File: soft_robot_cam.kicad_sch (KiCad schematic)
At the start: 76 parts, among them J1 Connector, J10 Screw_Terminal_01x02, J2 Conn_01x06, J3 Conn_01x03, J4 Conn_01x05_Pin, J5 Screw_Terminal_01x04, J6 Screw_Terminal_01x02, J7 Screw_Terminal_01x02, J8 Conn_01x24_Socket, J9 Screw_Terminal_01x02, Q1 S8050, Q2 S8050, Q3 AO3401A, SW1 SW_DIP_x02, SW3 SW_DP3T, SW4 SW_DIP_x02, SW5 SW_DP3T, U10 ICM-42605, U12 XC6206P282MR, U13 XC6206P122MR, U14 SY8113IADC, U3 MPU6500, U4 DRV8874PWPR, U5 DRV8874PWPR, U9 ESP32-S3-WROOM-1-N16R8

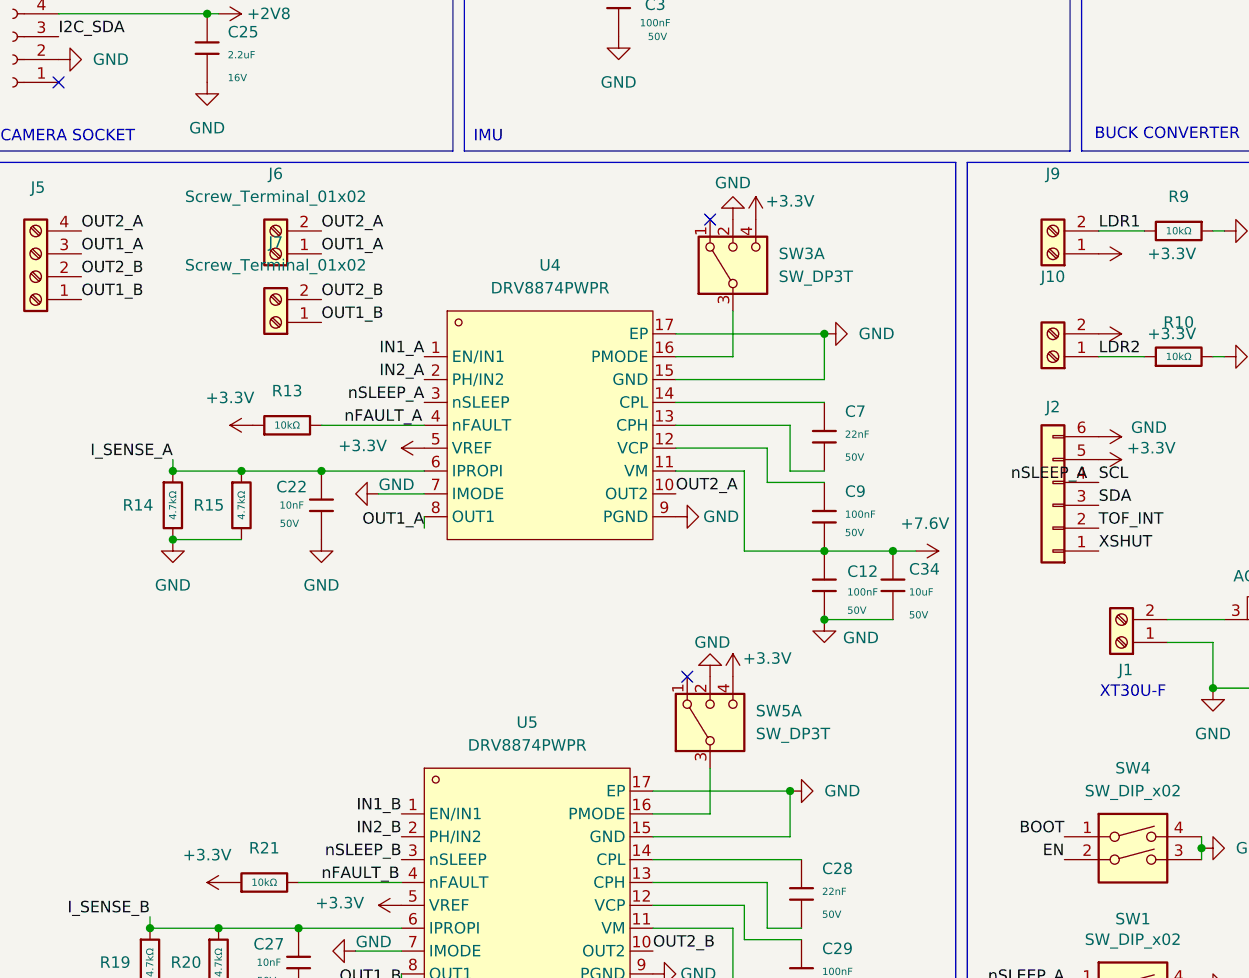
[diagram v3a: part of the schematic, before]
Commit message: Added most 3D models, revised some layout based off 3D model placement, need to verify JST-XH placement and ensure no design errors.
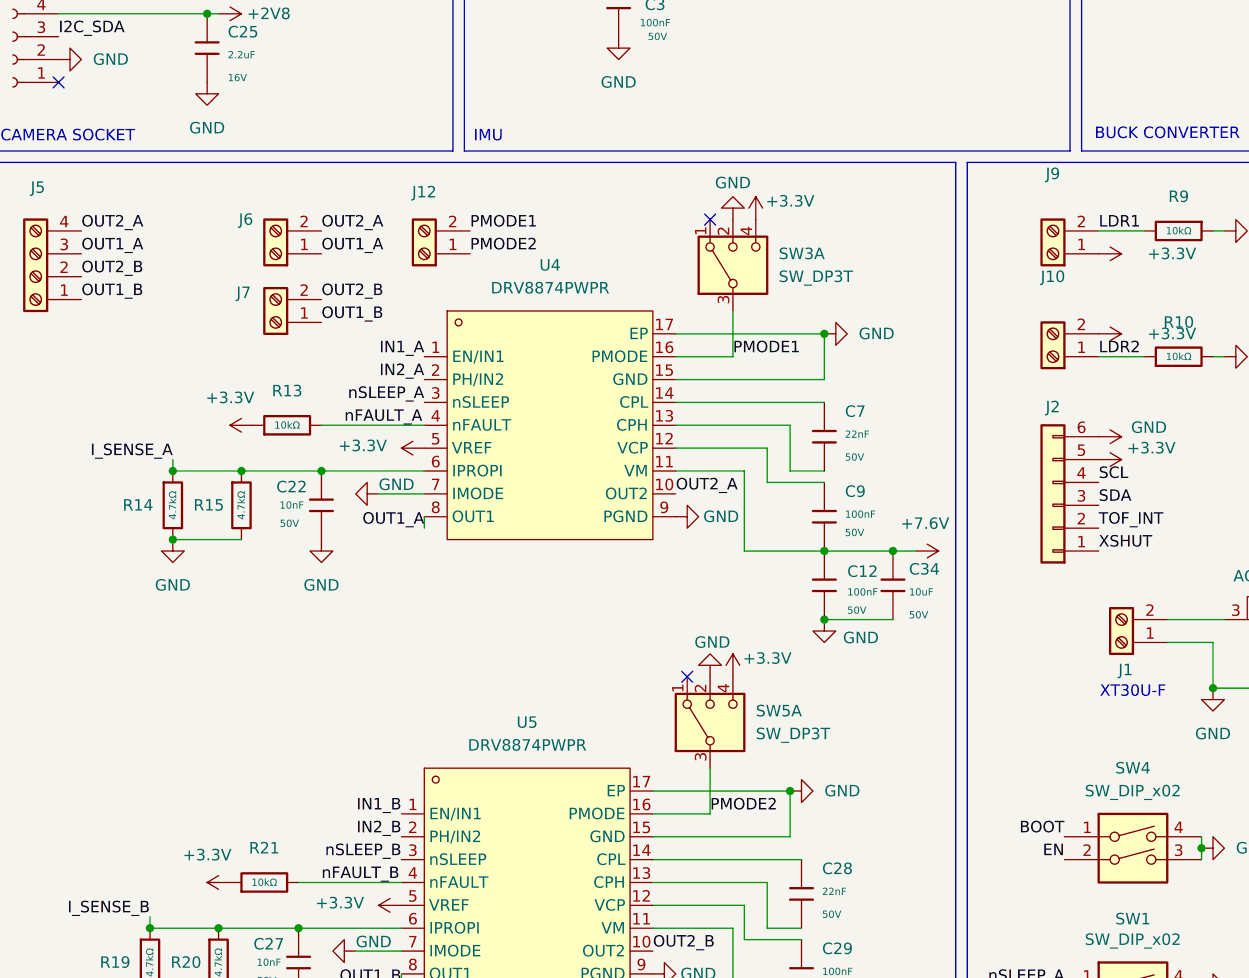
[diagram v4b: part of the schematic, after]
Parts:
- added J12: Screw_Terminal_01x02, Connector_PinHeader_1.00mm:PinHeader_1x02_P1.00mm_Vertical, symbol Connector:Screw_Terminal_01x02
- J1: LCSC (none) -> C99102
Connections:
- net PMODE1: now reaches SW3.3, U4.16 (PMODE)
- net PMODE1: now also J12.2 (Pin_2)
- net PMODE2: now reaches SW5.3, U5.16 (PMODE)
- net PMODE2: now also J12.1 (Pin_1)
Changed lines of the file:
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@@
 		)
 	)
+	(label "PMODE1"
+		(at 67.31 95.25 0)
+		(effects
+			(font
+				(size 1.27 1.27)
+			)
+			(justify left bottom)
+		)
+	)
 	(label "OUT1_B"
 		(at 59.69 179.07 180)
@@
 		)
 	)
+	(label "PMODE2"
+		(at 93.98 160.02 0)
+		(effects
+			(font
+				(size 1.27 1.27)
+			)
+			(justify left bottom)
+		)
+	)
 	(label "SCLK1"
 		(at 124.46 41.91 0)
@@
 		)
 	)
+	(label "PMODE1"
+		(at 96.52 109.22 0)
+		(effects
+			(font
+				(size 1.27 1.27)
+			)
+			(justify left bottom)
+		)
+	)
 	(label "HREF"
 		(at 220.98 111.76 180)
@@
 		)
 	)
-	(label "nSLEEP_A"
-		(at 135.89 123.19 180)
-		(effects
-			(font
-				(size 1.27 1.27)
-			)
-			(justify right bottom)
-		)
-	)
 	(label "BOOT"
 		(at 133.35 162.56 180)
@@
 		)
 	)
+	(label "PMODE2"
+		(at 67.31 97.79 0)
+		(effects
+			(font
+				(size 1.27 1.27)
+			)
+			(justify left bottom)
+		)
+	)
 	(label "Y3"
 		(at 21.59 27.94 0)
@@
 	)
 	(symbol
+		(lib_id "Connector:Screw_Terminal_01x02")
+		(at 62.23 97.79 180)
+		(unit 1)
+		(exclude_from_sim no)
+		(in_bom yes)
+		(on_board yes)
+		(dnp no)
+		(property "Reference" "J12"
+			(at 62.23 90.932 0)
+			(effects
+				(font
+					(size 1.27 1.27)
+				)
+			)
+		)
+		(property "Value" "Screw_Terminal_01x02"
+			(at 62.23 91.44 0)
+			(effects
+				(font
+					(size 1.27 1.27)
+				)
+				(hide yes)
+			)
+		)
+		(property "Footprint" "Connector_PinHeader_1.00mm:PinHeader_1x02_P1.00mm_Vertical"
+			(at 62.23 97.79 0)
+			(effects
+				(font
+					(size 1.27 1.27)
+				)
+				(hide yes)
+			)
+		)
+		(property "Datasheet" "~"
+			(at 62.23 97.79 0)
+			(effects
+				(font
+					(size 1.27 1.27)
+				)
+				(hide yes)
+			)
+		)
+		(property "Description" "Generic screw terminal, single row, 01x02, script generated (kicad-library-utils/schlib/autogen/connector/)"
+			(at 62.23 97.79 0)
+			(effects
+				(font
+					(size 1.27 1.27)
+				)
+				(hide yes)
+			)
+		)
+		(property "LCSC" ""
+			(at 62.23 97.79 0)
+			(effects
+				(font
+					(size 1.27 1.27)
+				)
+				(hide yes)
+			)
+		)
+		(pin "1"
+		)
+		(pin "2"
+		)
+		(instances
+			(project "soft_robot_cam"
+				(path "/8a7e5bec-e932-4403-8e68-78633cb41e92"
+					(reference "J12")
+					(unit 1)
+				)
+			)
+		)
+	)
+	(symbol
 		(lib_id "power:VD")
 		(at 163.83 119.38 270)
@@
 			)
 		)
+		(property "LCSC" "C99102"
+			(at 139.7 140.97 0)
+			(effects
+				(font
+					(size 1.27 1.27)
+				)
+				(hide yes)
+			)
+		)
 		(pin "1"
 		)
@@
 		(on_board yes)
 		(dnp no)
-		(fields_autoplaced yes)
 		(property "Reference" "J6"
-			(at 45.72 88.9 0)
+			(at 42.418 93.98 0)
 			(effects
 				(font
@@
 					(size 1.27 1.27)
 				)
+				(hide yes)
 			)
 		)
@@
 		(on_board yes)
 		(dnp no)
-		(fields_autoplaced yes)
 		(property "Reference" "J7"
-			(at 45.72 96.52 0)
+			(at 42.164 102.108 0)
 			(effects
 				(font
@@
 					(size 1.27 1.27)
 				)
+				(hide yes)
 			)
 		)

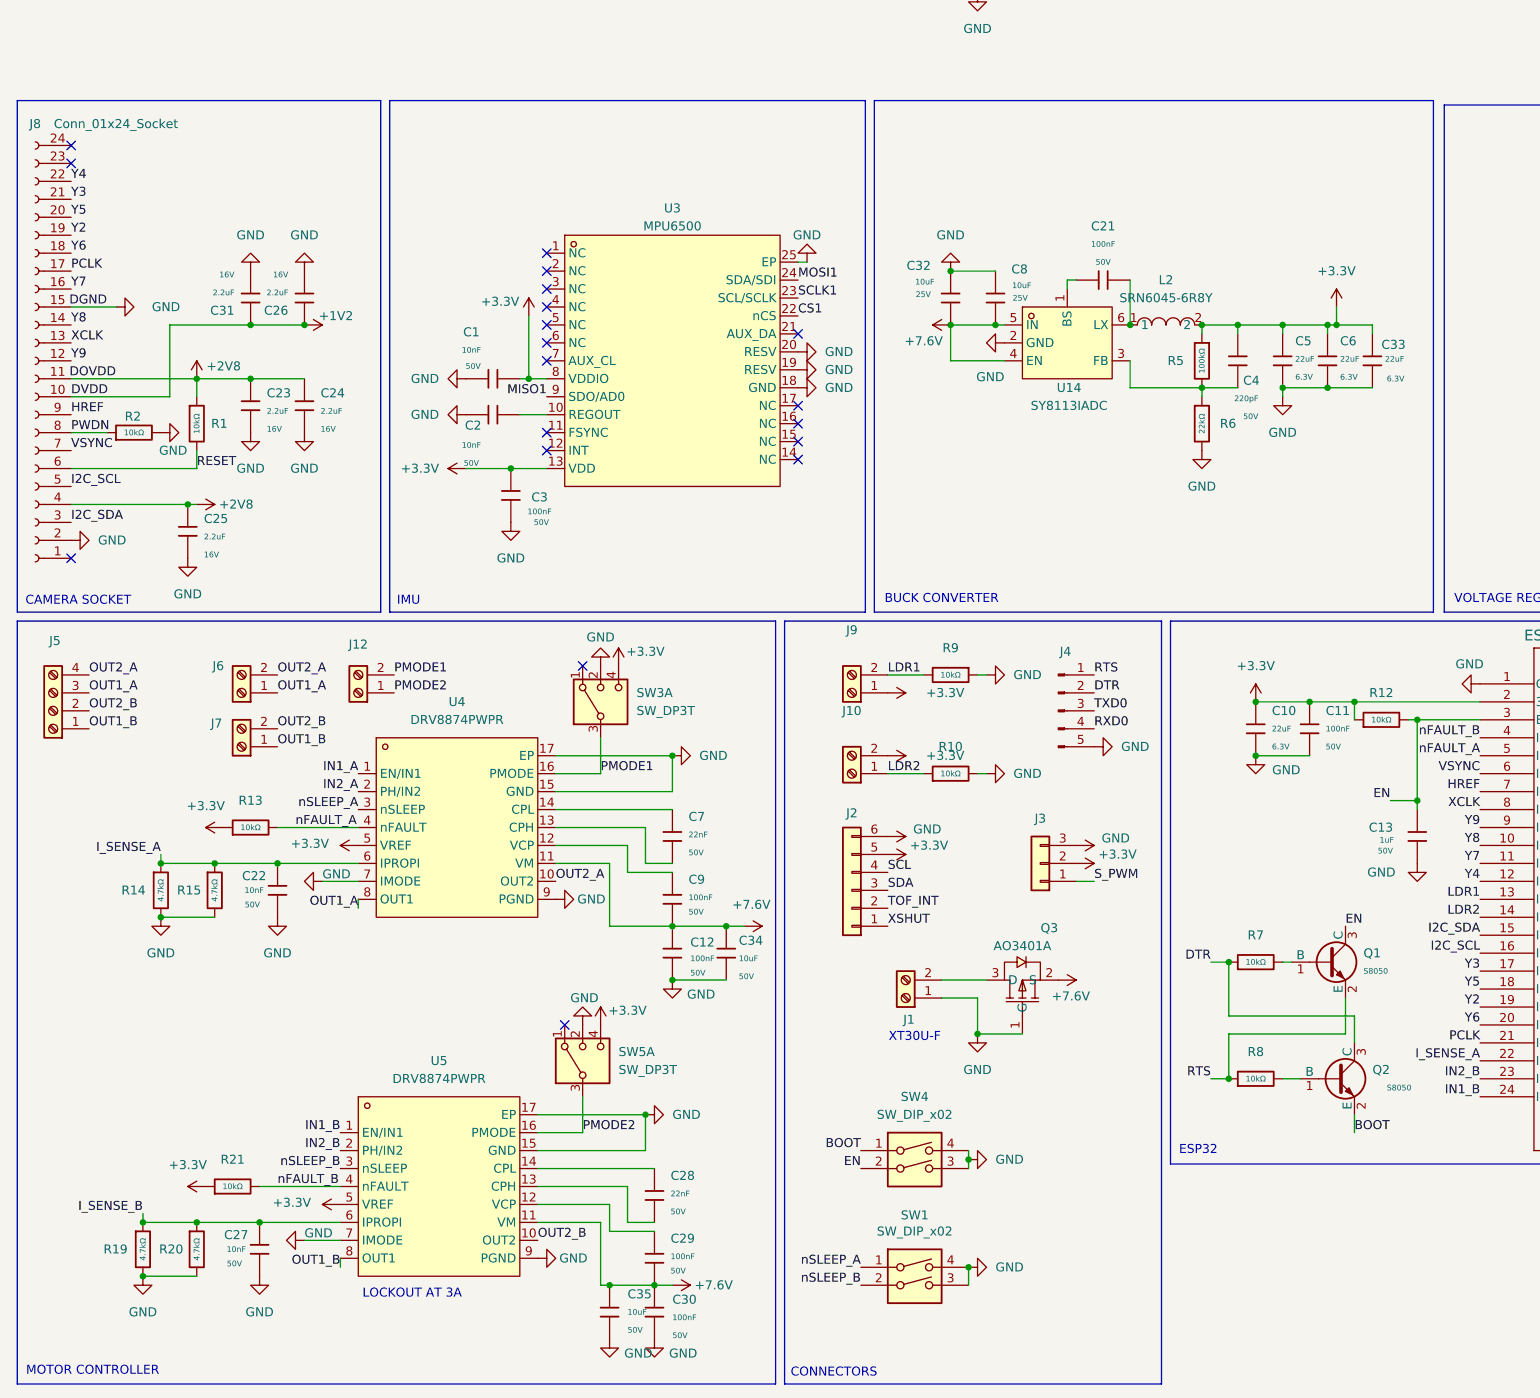
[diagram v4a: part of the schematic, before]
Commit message: Reviewed connector placement, chaning footprint to ensure clearance, added LEDs on Buck, slightly modified layout to improve spacing and clearance. Next is a full design and BOM review.
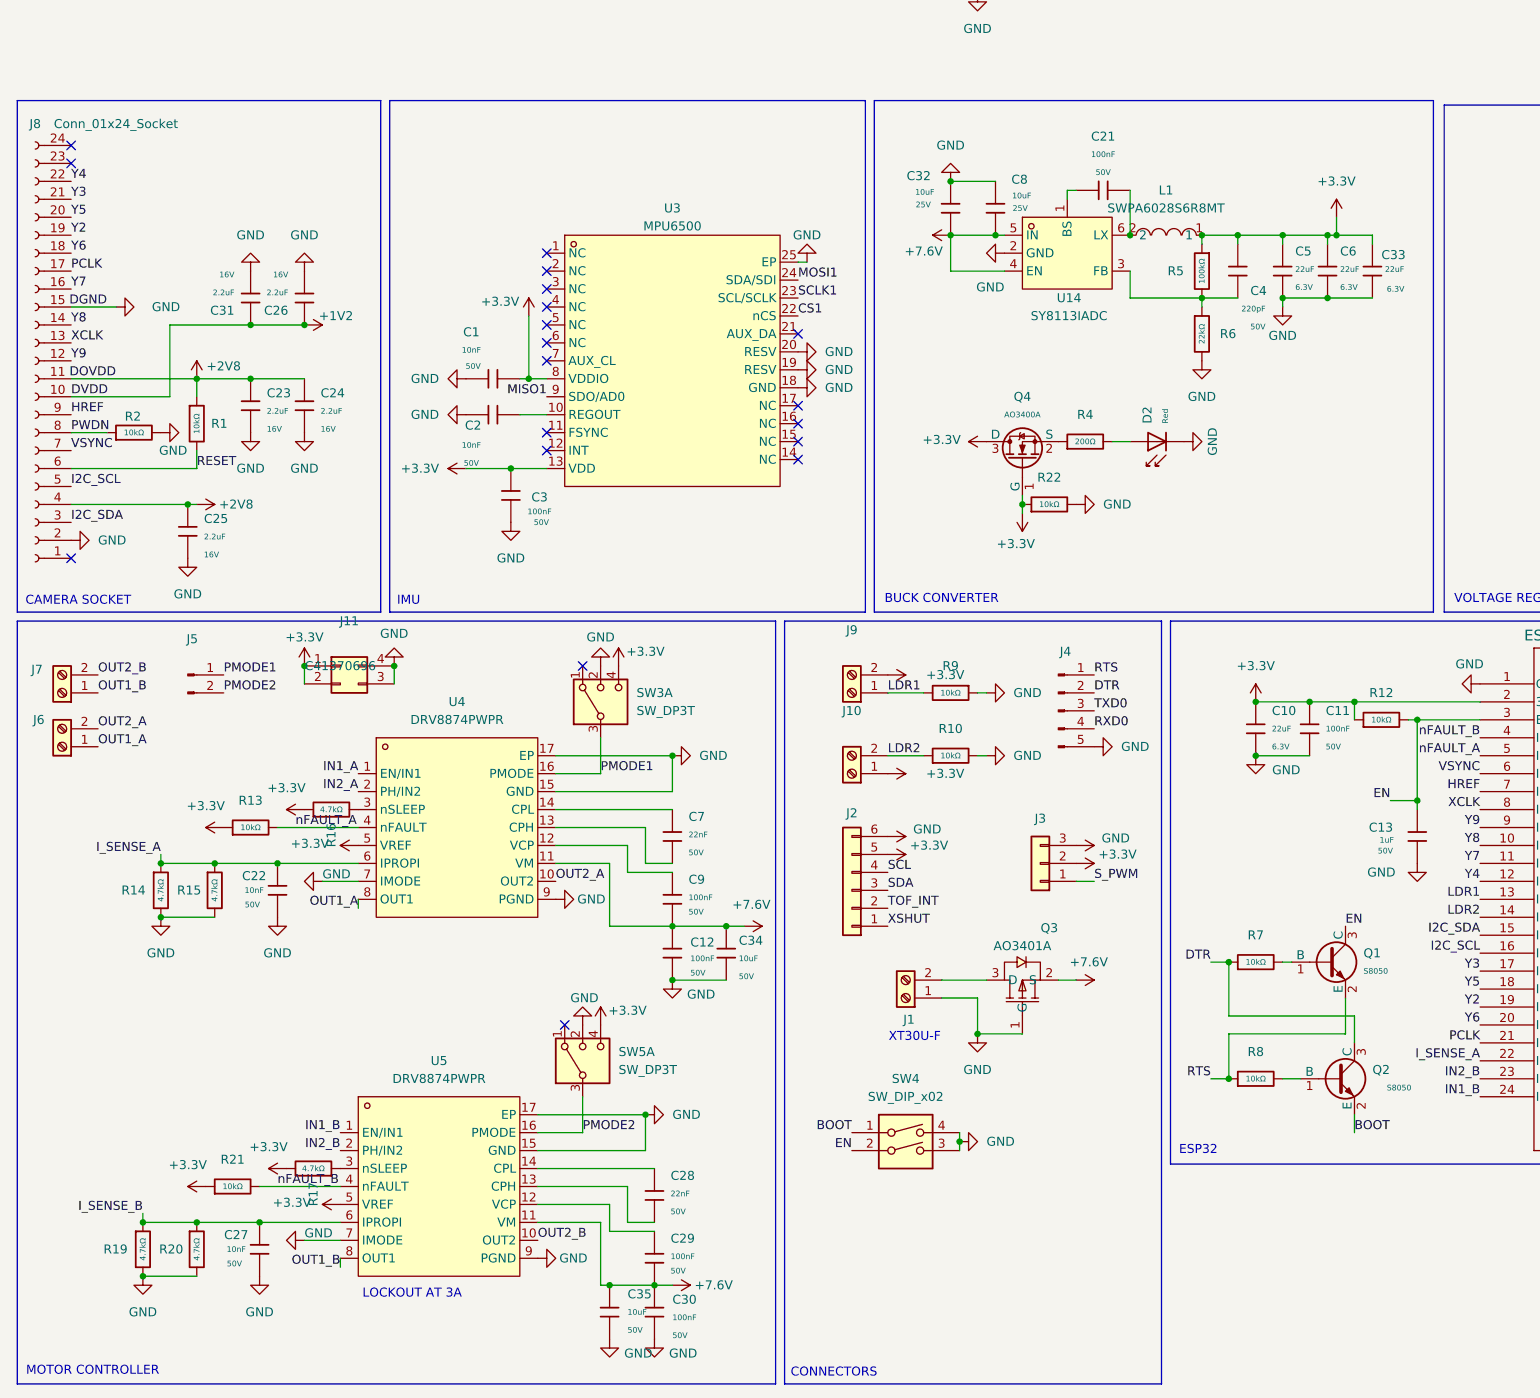
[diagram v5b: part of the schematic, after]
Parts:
- removed J12: Screw_Terminal_01x02, Connector_PinHeader_1.00mm:PinHeader_1x02_P1.00mm_Vertical, symbol Connector:Screw_Terminal_01x02
- removed J5: Screw_Terminal_01x04, PRETTY:CONN-TH_4P-P2.54_MX128-2.54-GN01-04P-CU-Y-A, symbol Connector:Screw_Terminal_01x04
- removed L2: SRN6045-6R8Y, easyeda2kicad:IND-SMD_L6.0-W6.0_SRN6045, symbol easyeda2kicad:SRN6045-6R8Y
- removed SW1: SW_DIP_x02, easyeda2kicad:SW-SMD_4P_DSHP02TSGET, symbol Switch:SW_DIP_x02
- added D2: Red, PCM_JLCPCB:D_0603, symbol PCM_JLCPCB-Diodes:LED,0603,Red
- added J11: Conn_02x02_Counter_Clockwise, Connector_PinHeader_1.00mm:PinHeader_2x02_P1.00mm_Vertical, symbol Connector_Generic:Conn_02x02_Counter_Clockwise
- added J5: Conn_01x02_Pin, easyeda2kicad:HDR-TH_2P-P1.27-V-M, symbol Connector:Conn_01x02_Pin
- added L1: SWPA6028S6R8MT, easyeda2kicad:IND-SMD_L6.0-W6.0_SWPA6045S, symbol easyeda2kicad:SWPA6028S6R8MT
- added Q4: AO3400A, PCM_JLCPCB:Q_SOT-23, symbol PCM_JLCPCB-Transistors:NMOS,AO3400A
- added R16, R17: 4.7kΩ, PCM_JLCPCB:R_0603, symbol PCM_JLCPCB-Resistors:0603,4.7kΩ
- added R22: 10kΩ, PCM_JLCPCB:R_0603, symbol PCM_JLCPCB-Resistors:0603,10kΩ
- added R4: 200Ω, PCM_JLCPCB:R_0402, symbol PCM_JLCPCB-Resistors:0402,200Ω
- J10, J6, J7, J9: footprint easyeda2kicad:CONN-TH_B2B-PH-K-S -> easyeda2kicad:JST_B2B-PH-K-S
- J4: LCSC (none) -> C5243685
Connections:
- net +3.3V: now also J10.1 (Pin_1), J9.2 (Pin_2), J11.1 (Pin_1), J11.2 (Pin_2), L1.1, Q4.1 (G), Q4.3 (D), R16.1, R17.2, R22.1; no longer J10.2 (Pin_2), J9.1 (Pin_1)
- net GND: now also D2.1, J11.3 (Pin_3), J11.4 (Pin_4), R22.2
- net LDR1: now also J9.1 (Pin_1); no longer J9.2 (Pin_2)
- net LDR2: now also J10.2 (Pin_2); no longer J10.1 (Pin_1)
- net PMODE1: now also J5.1 (Pin_1)
- net PMODE2: now also J5.2 (Pin_2)
- net at C21.2, U14.6 (LX): now also L1.2
- net nSLEEP_A: no longer names the net of U4.3 (nSLEEP)
- net nSLEEP_A: now also R16.2
- net nSLEEP_B: no longer names the net of U5.3 (nSLEEP)
- net nSLEEP_B: now also R17.1
- new net: D2.2, R4.2
- new net: Q4.2 (S), R4.1
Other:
- moved on the sheet: C21, C32, C33, C4, C5, C6, C8, J6, J7, R10, R5, R6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
